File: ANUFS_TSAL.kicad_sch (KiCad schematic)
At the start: 0 parts

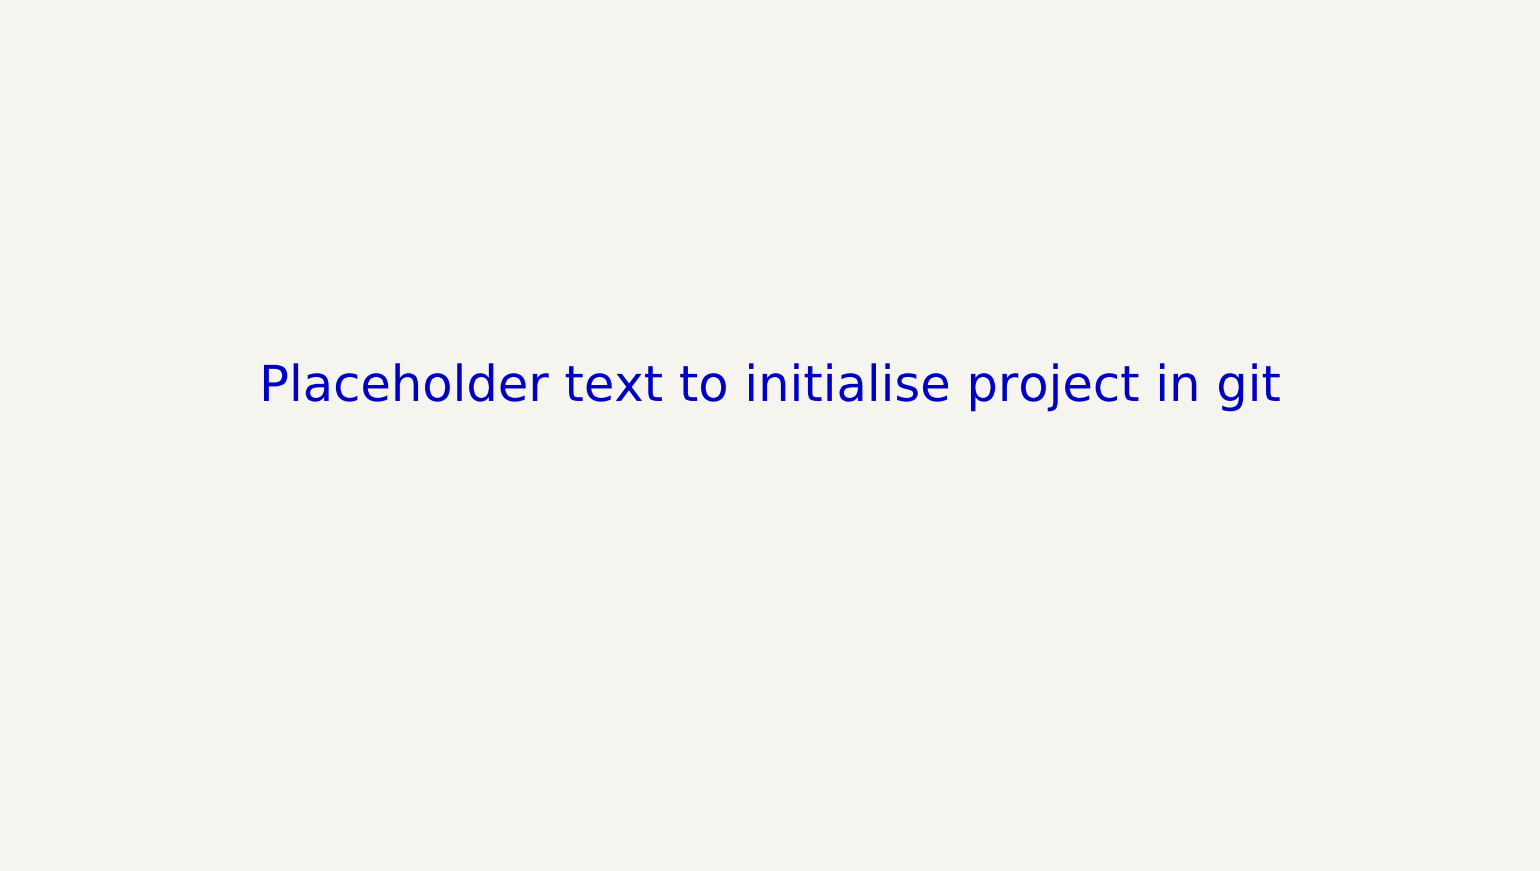
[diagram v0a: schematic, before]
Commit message: flash circuit complete, begin design of other components
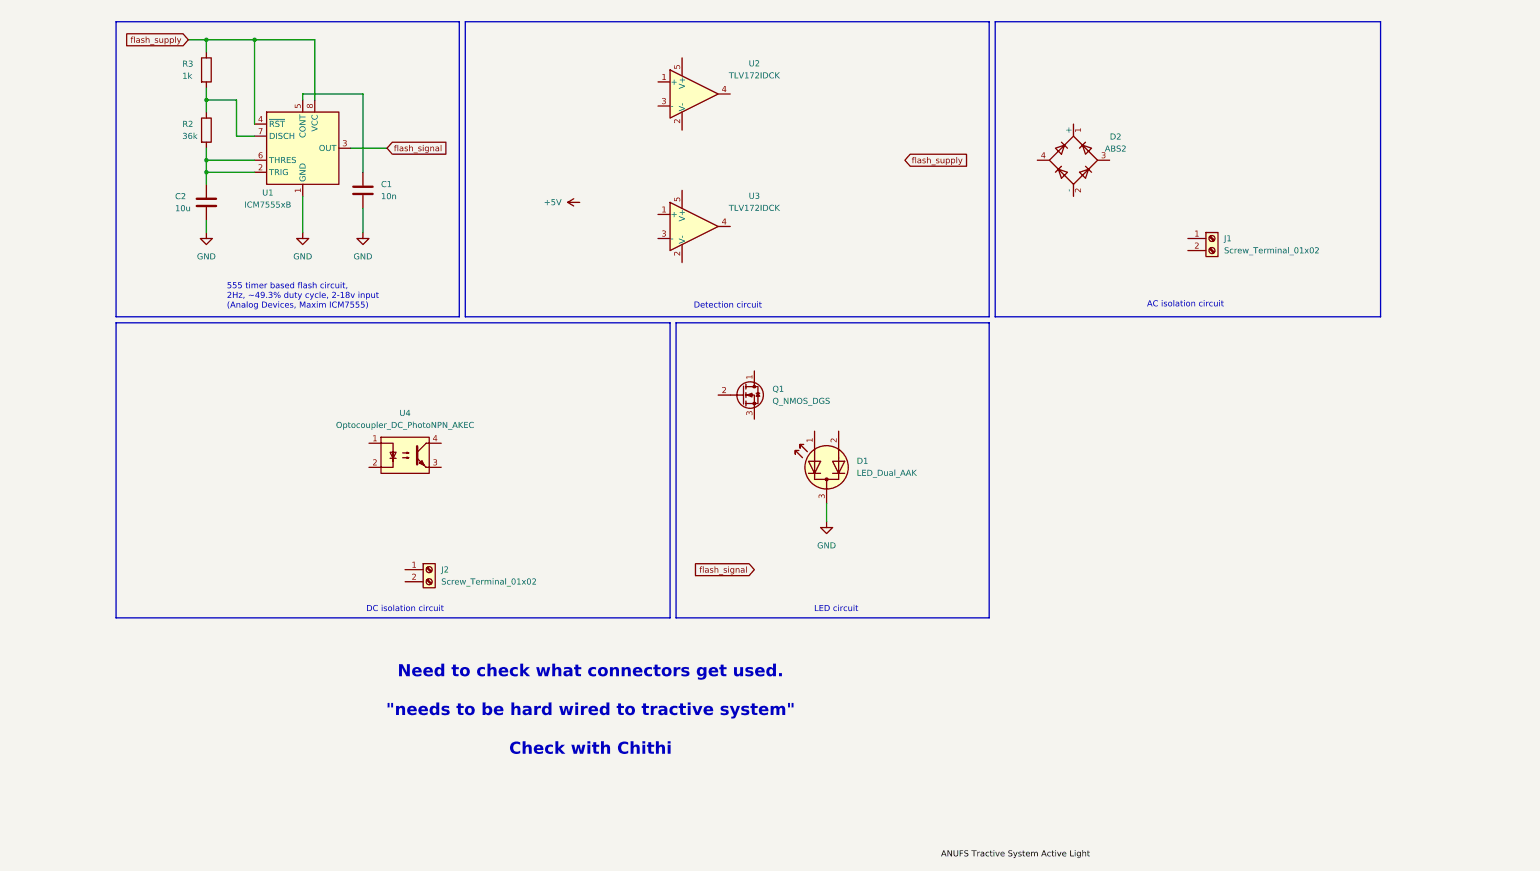
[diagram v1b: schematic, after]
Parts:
- added C1: 10n, symbol Device:C
- added C2: 10u, symbol Device:C
- added D1: LED_Dual_AAK, symbol Device:LED_Dual_AAK
- added D2: ABS2, Diode_SMD:Diode_Bridge_Diotec_ABS, symbol Diode_Bridge:ABS2
- added J1, J2: Screw_Terminal_01x02, symbol Connector:Screw_Terminal_01x02
- added Q1: Q_NMOS_DGS, symbol Transistor_FET:Q_NMOS_DGS
- added R2: 36k, symbol Device:R
- added R3: 1k, symbol Device:R
- added U1: ICM7555xB, Package_SO:SOIC-8_3.9x4.9mm_P1.27mm, symbol Timer:ICM7555xB
- added U2, U3: TLV172IDCK, Package_TO_SOT_SMD:SOT-353_SC-70-5, symbol Amplifier_Operational:TLV172IDCK
- added U4: Optocoupler_DC_PhotoNPN_AKEC, symbol Isolator:Optocoupler_DC_PhotoNPN_AKEC
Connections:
- new net: C2.1, R2.2, U1.2 (TRIG), U1.6 (THRES)
- new net: C1.1, U1.5 (CONT)
- new net: R2.1, R3.2, U1.7 (DISCH)
- new net GND: C1.2, C2.2, D1.3 (K), U1.1 (GND)
- new net flash_signal: U1.3 (OUT)
- new net flash_supply: R3.1, U1.4 (~{RST}), U1.8 (VCC)
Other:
- note added: "555 timer based flash circuit, 2Hz, ~49.3% duty cycle, 2-18v input (Analog Devices, Maxim ICM7555)"
- note added: "AC isolation circuit"
- note added: "DC isolation circuit"
- note added: "Detection circuit"
- note added: "LED circuit"
- note added: "Need to check what connectors get used. "needs to be hard wired to tractive system" Check with Chithi"
- note removed: "Placeholder text to initialise project in git"

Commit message: progress on AC detection, likely to change to full bridge rectification though
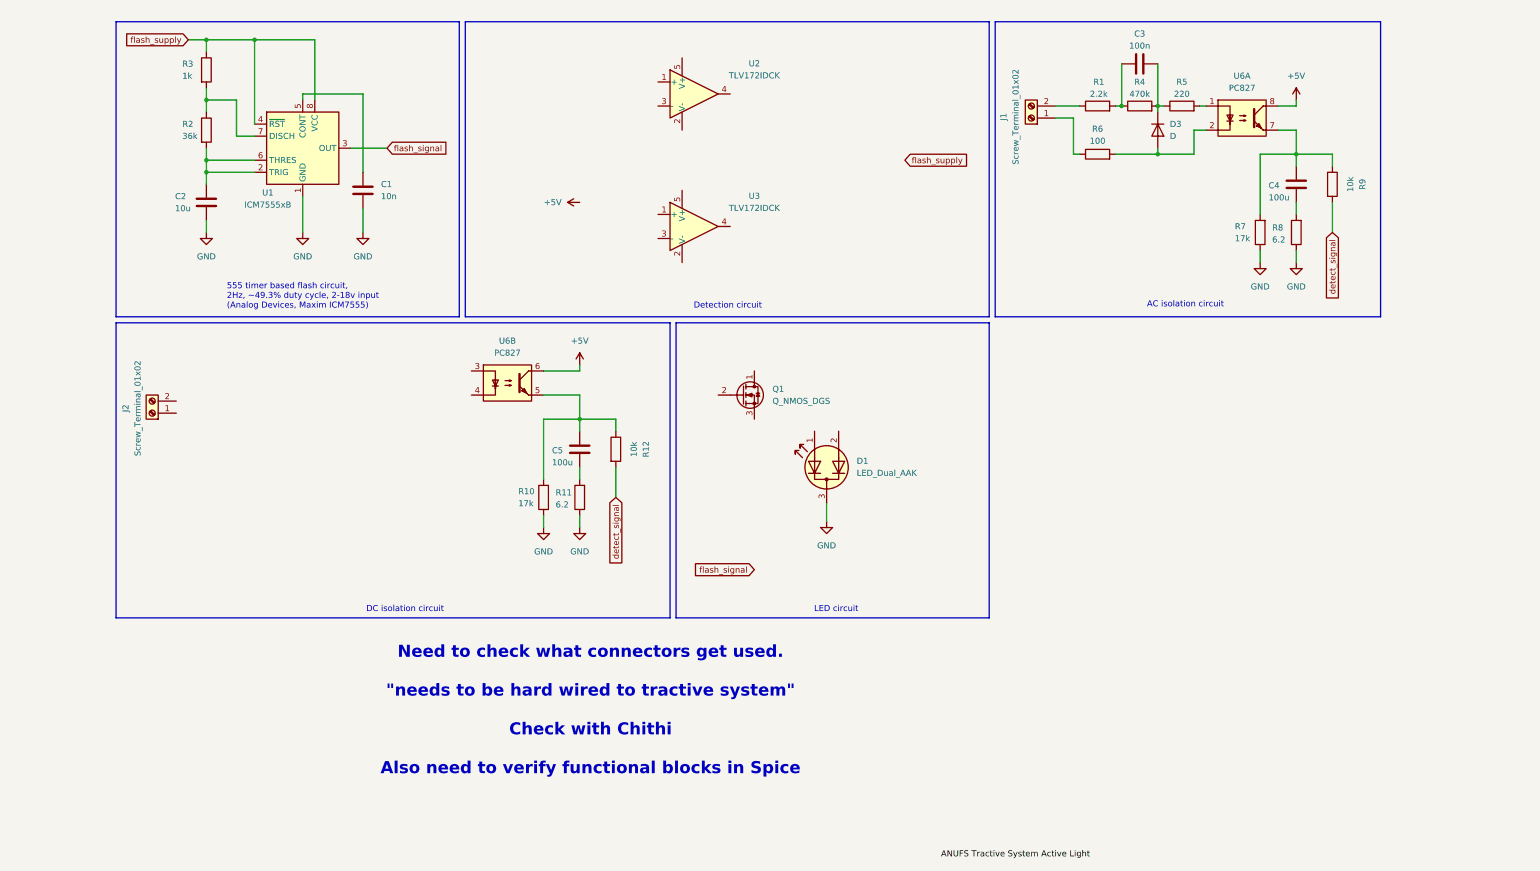
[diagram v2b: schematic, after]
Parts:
- removed D2: ABS2, Diode_SMD:Diode_Bridge_Diotec_ABS, symbol Diode_Bridge:ABS2
- removed U4: Optocoupler_DC_PhotoNPN_AKEC, symbol Isolator:Optocoupler_DC_PhotoNPN_AKEC
- added C3: 100n, symbol Device:C
- added C4, C5: 100u, symbol Device:C
- added D3: D, symbol Device:D
- added R1: 2.2k, symbol Device:R
- added R10, R7: 17k, symbol Device:R
- added R11, R8: 6.2, symbol Device:R
- added R12, R9: 10k, symbol Device:R
- added R4: 470k, symbol Device:R
- added R5: 220, symbol Device:R
- added R6: 100, symbol Device:R
- added U6: PC827, Package_DIP:DIP-8_W7.62mm, symbol Isolator:PC827
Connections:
- net +5V: now also U6.6, U6.8
- net GND: now also R10.1, R11.1, R7.1, R8.1
- net at J1.1 (Pin_1): now also R6.1
- net at J1.2 (Pin_2): now also R1.1
- new net: C3.1, D3.1 (K), R4.2, R5.1
- new net: D3.2 (A), R6.2, U6.2
- new net: C5.2, R11.2
- new net: R5.2, U6.1
- new net: C4.1, R7.2, R9.1, U6.7
- new net: C3.2, R1.2, R4.1
- new net: C5.1, R10.2, R12.1, U6.5
- new net: C4.2, R8.2
- new net detect_signal: R12.2, R9.2
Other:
- note added: "Need to check what connectors get used. "needs to be hard wired to tractive system" Check with Chithi Also need to verify functional blocks in Spice"
- note removed: "Need to check what connectors get used. "needs to be hard wired to tractive system" Check with Chithi"
- moved on the sheet: J1, J2

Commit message: Design idea complete, need to select components/set values/set footprints
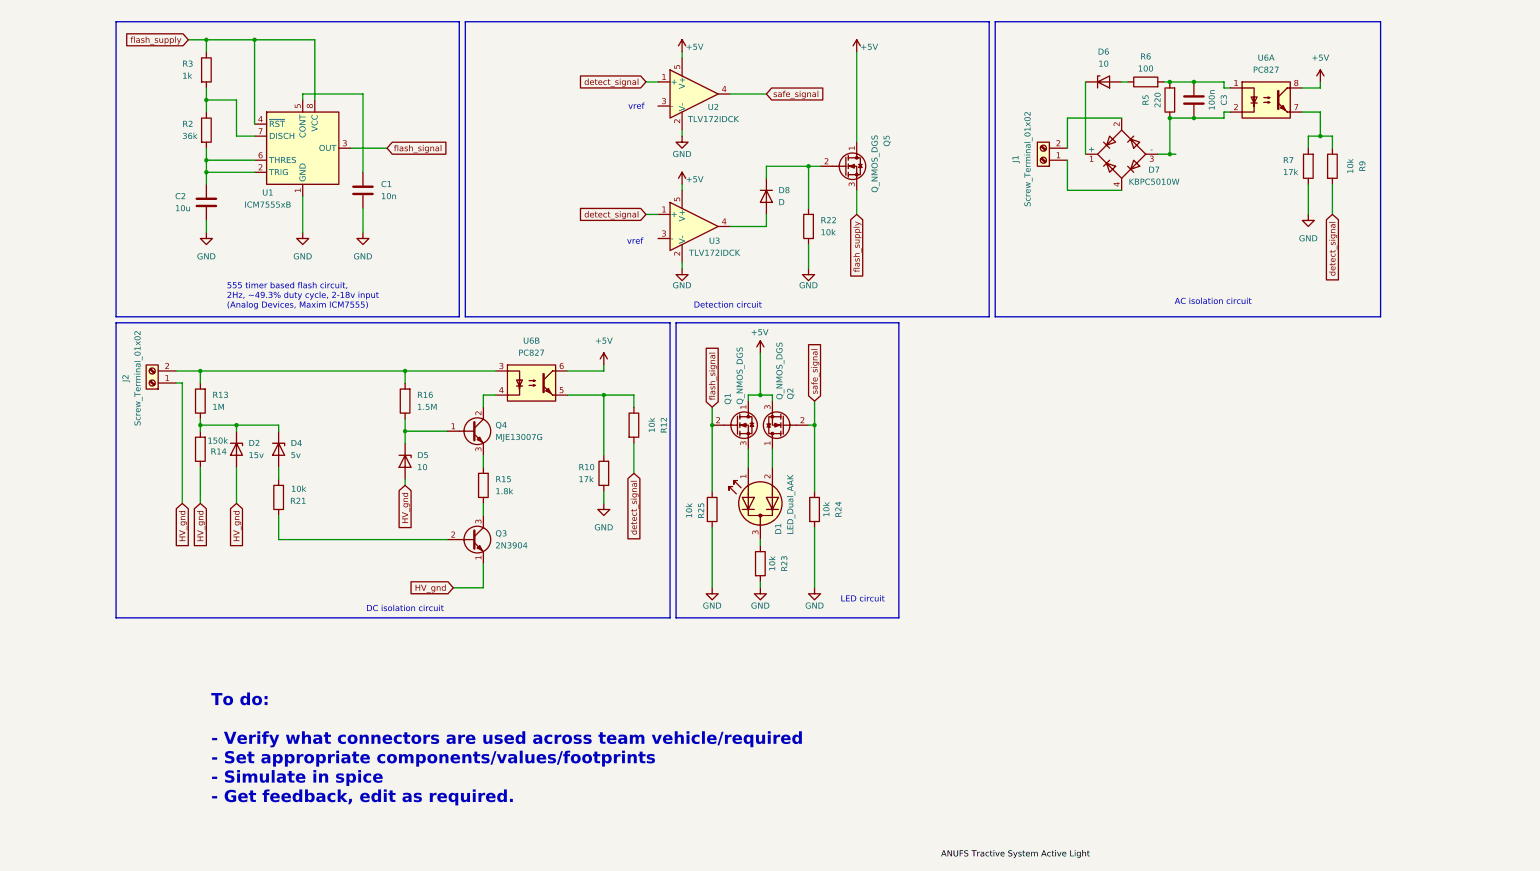
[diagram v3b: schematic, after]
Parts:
- removed C4, C5: 100u, symbol Device:C
- removed D3: D, symbol Device:D
- removed R1: 2.2k, symbol Device:R
- removed R11, R8: 6.2, symbol Device:R
- removed R4: 470k, symbol Device:R
- added D2: 15v, symbol Device:D_Zener
- added D4: 5v, symbol Device:D_Zener
- added D5, D6: 10, symbol Device:D_Zener
- added D7: KBPC5010W, Diode_THT:Diode_Bridge_GeneSiC_KBPC_W, symbol Diode_Bridge:KBPC5010W
- added D8: D, symbol Device:D
- added Q2, Q5: Q_NMOS_DGS, symbol Transistor_FET:Q_NMOS_DGS
- added Q3: 2N3904, Package_TO_SOT_THT:TO-92_Inline, symbol Transistor_BJT:2N3904
- added Q4: MJE13007G, Package_TO_SOT_THT:TO-220-3_Vertical, symbol Transistor_BJT:MJE13007G
- added R13: 1M, symbol Device:R
- added R14: 150k, symbol Device:R
- added R15: 1.8k, symbol Device:R
- added R16: 1.5M, symbol Device:R
- added R21, R22, R23, R24, R25: 10k, symbol Device:R
- added unit 1 of U6
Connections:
- net +5V: now also Q1.1 (D), U2.5 (V+), U3.5 (V+), Q2.3 (S), Q5.1 (D), U6.8; no longer U6.8
- net GND: now also U2.2 (V-), U3.2 (V-), R22.1, R23.2, R24.2, R25.2; no longer D1.3 (K)
- net detect_signal: now also U2.1 (+), U3.1 (+)
- net flash_signal: now also Q1.2 (G), R25.1
- net flash_supply: now also Q5.3 (S)
- net HV_gnd: now reaches J2.1 (Pin_1)
- net HV_gnd: now also D2.2 (A), D5.2 (A), Q3.1 (E), R14.1
- net at J2.2 (Pin_2): now also U6.3, R13.2, R16.2
- net at U3.4: now also D8.2 (A)
- net at C3.1, R5.1: now also D7.3 (-), U6.2
- net at R6.2: now also C3.2, R5.2, U6.1; no longer U6.2
- net at R7.2, R9.1: now also U6.7; no longer U6.7
- net at J1.1 (Pin_1): now also D7.4; no longer R6.1
- net at J1.2 (Pin_2): now also D7.2
- net at Q1.3 (S): now also D1.1 (A1)
- net safe_signal: now reaches U2.4
- net safe_signal: now also Q2.2 (G), R24.1
- net at D1.2 (A2): now also Q2.1 (D)
- net at U6.4: now also Q4.2 (C)
- new net: D8.1 (K), Q5.2 (G), R22.2
- new net: D5.1 (K), Q4.1 (B), R16.1
- new net: D1.3 (K), R23.1
- new net: Q3.2 (B), R21.1
- new net: D4.2 (A), R21.2
- new net: D2.1 (K), D4.1 (K), R13.1, R14.2
- new net: Q3.3 (C), R15.1
- new net: Q4.3 (E), R15.2
- new net: D6.2 (A), R6.1
- new net: D6.1 (K), D7.1 (+)
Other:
- note added: "To do: - Verify what connectors are used across team vehicle/required - Set appropriate components/values/footprints - Simulate in spice - Get feedback, edit as required."
- note added: "vref"
- note removed: "Need to check what connectors get used. "needs to be hard wired to tractive system" Check with Chithi Also need to verify functional blocks in Spice"
- moved on the sheet: J1, J2, R10, R12, R7, R9, U6B

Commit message: Remaining simulation to complete is for AC detection
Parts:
- removed D8: D, symbol Device:D
- added R1: 2.2k, symbol Device:R
- added R4: 10k, symbol Device:R
- R23: value 10k -> 100
- R24, R25: value 10k -> 22k
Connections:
- net +5V: now also R1.1
- net GND: now also R4.2
- net at Q5.2 (G), R22.2: now also U3.4
- net at U3.3 (-): now also U2.3 (-), R1.2, R4.1

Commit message: woopsie had kicad locking the file lol
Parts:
- R22: value 10k -> 22k
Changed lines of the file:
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@@
 	)
 	(junction
-		(at 234.95 41.91)
-		(diameter 0)
-		(color 0 0 0 0)
-	)
-	(junction
 		(at 73.66 100.33)
 		(diameter 0)
@@
 	(wire
 		(pts
-			(xy 234.95 41.91) (xy 236.22 41.91)
-		)
-		(stroke
-			(width 0)
-			(type default)
-		)
-	)
-	(wire
-		(pts
 			(xy 213.36 34.29) (xy 224.79 34.29)
 		)
@@
 			)
 		)
-		(property "Value" "10k"
+		(property "Value" "22k"
 			(at 161.29 58.4199 0)
 			(show_name no)

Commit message: finish schematic
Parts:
- removed C3: 100n, symbol Device:C
- removed D6: 10, symbol Device:D_Zener
- removed D7: KBPC5010W, Diode_THT:Diode_Bridge_GeneSiC_KBPC_W, symbol Diode_Bridge:KBPC5010W
- removed J1: Screw_Terminal_01x02, symbol Connector:Screw_Terminal_01x02
- removed R5: 220, symbol Device:R
- removed R6: 100, symbol Device:R
- removed R7: 17k, symbol Device:R
- removed R9: 10k, symbol Device:R
- removed U6: PC827, Package_DIP:DIP-8_W7.62mm, symbol Isolator:PC827
- added U4: Optocoupler_DC_PhotoNPN_AKEC, symbol Isolator:Optocoupler_DC_PhotoNPN_AKEC
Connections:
- net +5V: now also U4.4
- net at J2.2 (Pin_2), R13.2, R16.2: now also U4.1
- net at R10.2, R12.1: now also U4.3
- net at Q4.2 (C): now also U4.2
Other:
- note added: "ANUFS Tractive System Active Light (TSAL)"
- note removed: "AC isolation circuit"
- note removed: "To do: - Verify what connectors are used across team vehicle/required - Set appropriate components/values/footprints - Simulate in spice - Get feedback, edit as required."
- moved on the sheet: D2, D4, D5, J2, Q1, Q2, Q3, Q4, R10, R12, R13, R14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

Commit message: component footprint selection complete
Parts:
- removed J2: Screw_Terminal_01x02, symbol Connector:Screw_Terminal_01x02
- removed Q3: 2N3904, Package_TO_SOT_THT:TO-92_Inline, symbol Transistor_BJT:2N3904
- removed Q4: MJE13007G, Package_TO_SOT_THT:TO-220-3_Vertical, symbol Transistor_BJT:MJE13007G
- added Q4: NPN, Package_TO_SOT_SMD:TO-252-3_TabPin2, symbol Simulation_SPICE:NPN
- added Q6: NPN, Package_TO_SOT_SMD:SOT-23, symbol Simulation_SPICE:NPN
- C1: footprint (none) -> Capacitor_SMD:C_0805_2012Metric
- C2: footprint (none) -> Capacitor_SMD:C_Elec_10x10.2
- D1: footprint (none) -> LED_THT:LED_D10.0mm-3
- D2, D4, D5: footprint (none) -> Diode_SMD:D_SOD-323_HandSoldering
- Q1, Q2, Q5: footprint (none) -> Package_TO_SOT_SMD:TSOT-23
- R1, R10, R12, R13, R14, R15, R16, R2, R21, R22, R23, R24, R25, R3, R4: footprint (none) -> Resistor_SMD:R_0805_2012Metric
- U4: footprint (none) -> OptoDevice:Everlight_ITR1201SR10AR
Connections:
- net HV_gnd: now also Q6.3 (E)
- net at D5.1 (K), R16.1: now also Q4.2 (B)
- net at R21.1: now also Q6.2 (B)
- net HV_in: now reaches R13.2, R16.2, U4.1
- net at U4.2: now also Q4.1 (C)
- net at R15.1: now also Q6.1 (C)
- net at R15.2: now also Q4.3 (E)
